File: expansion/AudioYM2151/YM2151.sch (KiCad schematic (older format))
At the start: 17 parts, among them U3 LTC690x, U4 YM2151, U5 YM3012, U6 TL064

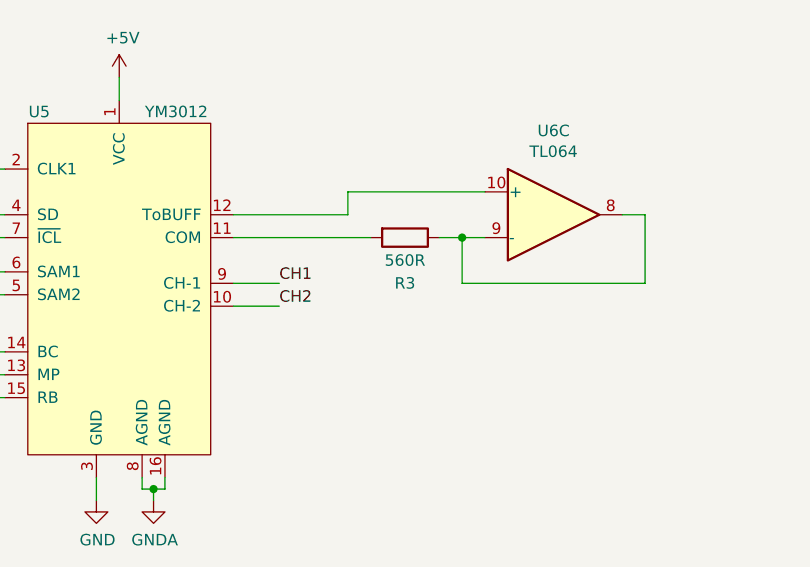
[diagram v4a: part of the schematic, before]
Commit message: Re-started layout on YM2151 board
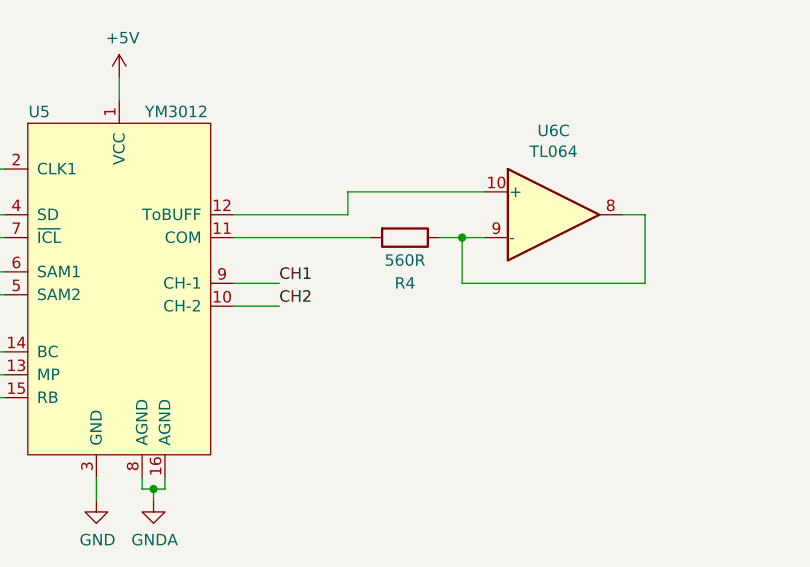
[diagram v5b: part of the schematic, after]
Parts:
- renumbered R3 to R4
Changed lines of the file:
@@
 $EndComp
 $Comp
-L Device:R R3
+L Device:R R4
 U 1 1 60BAB26A
 P 7800 4550
-F 0 "R3" V 8000 4550 50  0000 C CNN
+F 0 "R4" V 8000 4550 50  0000 C CNN
 F 1 "560R" V 7900 4550 50  0000 C CNN
 F 2 "Resistor_THT:R_Axial_DIN0207_L6.3mm_D2.5mm_P10.16mm_Horizontal" V 7730 4550 50  0001 C CNN
@@
 	2050 5450 2300 5450
 $Comp
-L power:+5V #PWR030
+L power:+5V #PWR031
 U 1 1 60C08870
 P 2750 3800
-F 0 "#PWR030" H 2750 3650 50  0001 C CNN
+F 0 "#PWR031" H 2750 3650 50  0001 C CNN
 F 1 "+5V" H 2765 3973 50  0000 C CNN
 F 2 "" H 2750 3800 50  0001 C CNN
@@
 $EndComp
 $Comp
-L power:GND #PWR031
+L power:GND #PWR032
 U 1 1 60C08E24
 P 2750 5850
-F 0 "#PWR031" H 2750 5600 50  0001 C CNN
+F 0 "#PWR032" H 2750 5600 50  0001 C CNN
 F 1 "GND" H 2755 5677 50  0000 C CNN
 F 2 "" H 2750 5850 50  0001 C CNN
@@
 $EndComp
 $Comp
-L power:GND #PWR040
+L power:GND #PWR041
 U 1 1 60C0A870
 P 6450 5700
-F 0 "#PWR040" H 6450 5450 50  0001 C CNN
+F 0 "#PWR041" H 6450 5450 50  0001 C CNN
 F 1 "GND" H 6455 5527 50  0000 C CNN
 F 2 "" H 6450 5700 50  0001 C CNN
@@
 	2750 5800 2800 5800
 $Comp
-L power:+5V #PWR041
+L power:+5V #PWR042
 U 1 1 60C9B598
 P 6550 3850
-F 0 "#PWR041" H 6550 3700 50  0001 C CNN
+F 0 "#PWR042" H 6550 3700 50  0001 C CNN
 F 1 "+5V" H 6565 4023 50  0000 C CNN
 F 2 "" H 6550 3850 50  0001 C CNN
@@
 $EndComp
 $Comp
-L power:+5V #PWR028
+L power:+5V #PWR029
 U 1 1 60CD204F
 P 2750 2000
-F 0 "#PWR028" H 2750 1850 50  0001 C CNN
+F 0 "#PWR029" H 2750 1850 50  0001 C CNN
 F 1 "+5V" H 2765 2173 50  0000 C CNN
 F 2 "" H 2750 2000 50  0001 C CNN
@@
 $EndComp
 $Comp
-L power:GND #PWR029
+L power:GND #PWR030
 U 1 1 60CD264A
 P 2750 3200
-F 0 "#PWR029" H 2750 2950 50  0001 C CNN
+F 0 "#PWR030" H 2750 2950 50  0001 C CNN
 F 1 "GND" H 2755 3027 50  0000 C CNN
 F 2 "" H 2750 3200 50  0001 C CNN
@@
 	5100 4250 6050 4250
 $Comp
-L power:+5V #PWR036
+L power:+5V #PWR037
 U 1 1 60D62AD7
 P 4700 3250
-F 0 "#PWR036" H 4700 3100 50  0001 C CNN
+F 0 "#PWR037" H 4700 3100 50  0001 C CNN
 F 1 "+5V" H 4715 3423 50  0000 C CNN
 F 2 "" H 4700 3250 50  0001 C CNN
@@
 $EndComp
 $Comp
-L power:GND #PWR033
+L power:GND #PWR034
 U 1 1 6153751F
 P 3300 3200
-F 0 "#PWR033" H 3300 2950 50  0001 C CNN
+F 0 "#PWR034" H 3300 2950 50  0001 C CNN
 F 1 "GND" H 3305 3027 50  0000 C CNN
 F 2 "" H 3300 3200 50  0001 C CNN
@@
 $EndComp
 $Comp
-L power:+5V #PWR032
+L power:+5V #PWR033
 U 1 1 61537D3F
 P 3300 2000
-F 0 "#PWR032" H 3300 1850 50  0001 C CNN
+F 0 "#PWR033" H 3300 1850 50  0001 C CNN
 F 1 "+5V" H 3315 2173 50  0000 C CNN
 F 2 "" H 3300 2000 50  0001 C CNN
@@
 	3300 2700 3300 2800
 $Comp
-L power:GNDA #PWR042
+L power:GNDA #PWR043
 U 1 1 61042847
 P 6700 5700
-F 0 "#PWR042" H 6700 5450 50  0001 C CNN
+F 0 "#PWR043" H 6700 5450 50  0001 C CNN
 F 1 "GNDA" H 6705 5527 50  0000 C CNN
 F 2 "" H 6700 5700 50  0001 C CNN
@@
 $EndComp
 $Comp
-L power:GNDA #PWR046
+L power:GNDA #PWR047
 U 1 1 61042C03
 P 9700 5750
-F 0 "#PWR046" H 9700 5500 50  0001 C CNN
+F 0 "#PWR047" H 9700 5500 50  0001 C CNN
 F 1 "GNDA" H 9705 5577 50  0000 C CNN
 F 2 "" H 9700 5750 50  0001 C CNN
@@
 $EndComp
 $Comp
-L power:GNDA #PWR043
+L power:GNDA #PWR044
 U 1 1 610435DB
 P 8150 1750
-F 0 "#PWR043" H 8150 1500 50  0001 C CNN
+F 0 "#PWR044" H 8150 1500 50  0001 C CNN
 F 1 "GNDA" H 8155 1577 50  0000 C CNN
 F 2 "" H 8150 1750 50  0001 C CNN
@@
 $EndComp
 $Comp
-L power:GNDA #PWR044
+L power:GNDA #PWR045
 U 1 1 61043A6E
 P 8150 3050
-F 0 "#PWR044" H 8150 2800 50  0001 C CNN
+F 0 "#PWR045" H 8150 2800 50  0001 C CNN
 F 1 "GNDA" H 8155 2877 50  0000 C CNN
 F 2 "" H 8150 3050 50  0001 C CNN
@@
 $EndComp
 $Comp
-L power:GNDA #PWR039
+L power:GNDA #PWR040
 U 1 1 61043CBD
 P 5750 2350
-F 0 "#PWR039" H 5750 2100 50  0001 C CNN
+F 0 "#PWR040" H 5750 2100 50  0001 C CNN
 F 1 "GNDA" H 5755 2177 50  0000 C CNN
 F 2 "" H 5750 2350 50  0001 C CNN
@@
 	3650 6450 3650 6550
 $Comp
-L power:GNDA #PWR035
+L power:GNDA #PWR036
 U 1 1 61044112
 P 3650 7150
-F 0 "#PWR035" H 3650 6900 50  0001 C CNN
+F 0 "#PWR036" H 3650 6900 50  0001 C CNN
 F 1 "GNDA" H 3655 6977 50  0000 C CNN
 F 2 "" H 3650 7150 50  0001 C CNN
@@
 P 5350 7150
 AR Path="/60D530A5/60EA6620" Ref="#PWR?"  Part="1"
-AR Path="/60B0BE0A/60EA6620" Ref="#PWR038"  Part="1"
-F 0 "#PWR038" H 5350 6900 50  0001 C CNN
+AR Path="/60B0BE0A/60EA6620" Ref="#PWR039"  Part="1"
+F 0 "#PWR039" H 5350 6900 50  0001 C CNN
 F 1 "GND" H 5355 6977 50  0000 C CNN
 F 2 "" H 5350 7150 50  0001 C CNN
@@
 P 5350 6450
 AR Path="/60D530A5/60EA6626" Ref="#PWR?"  Part="1"
-AR Path="/60B0BE0A/60EA6626" Ref="#PWR037"  Part="1"
-F 0 "#PWR037" H 5350 6300 50  0001 C CNN
+AR Path="/60B0BE0A/60EA6626" Ref="#PWR038"  Part="1"
+F 0 "#PWR038" H 5350 6300 50  0001 C CNN
 F 1 "+5V" H 5365 6623 50  0000 C CNN
 F 2 "" H 5350 6450 50  0001 C CNN
@@
 P 3650 6450
 AR Path="/60D530A5/6115823E" Ref="#PWR?"  Part="1"
-AR Path="/60B0BE0A/6115823E" Ref="#PWR0101"  Part="1"
-F 0 "#PWR0101" H 3650 6300 50  0001 C CNN
+AR Path="/60B0BE0A/6115823E" Ref="#PWR035"  Part="1"
+F 0 "#PWR035" H 3650 6300 50  0001 C CNN
 F 1 "+5V" H 3665 6623 50  0000 C CNN
 F 2 "" H 3650 6450 50  0001 C CNN
@@
 P 9700 4950
 AR Path="/60D530A5/61158651" Ref="#PWR?"  Part="1"
-AR Path="/60B0BE0A/61158651" Ref="#PWR0102"  Part="1"
-F 0 "#PWR0102" H 9700 4800 50  0001 C CNN
+AR Path="/60B0BE0A/61158651" Ref="#PWR046"  Part="1"
+F 0 "#PWR046" H 9700 4800 50  0001 C CNN
 F 1 "+5V" H 9715 5123 50  0000 C CNN
 F 2 "" H 9700 4950 50  0001 C CNN

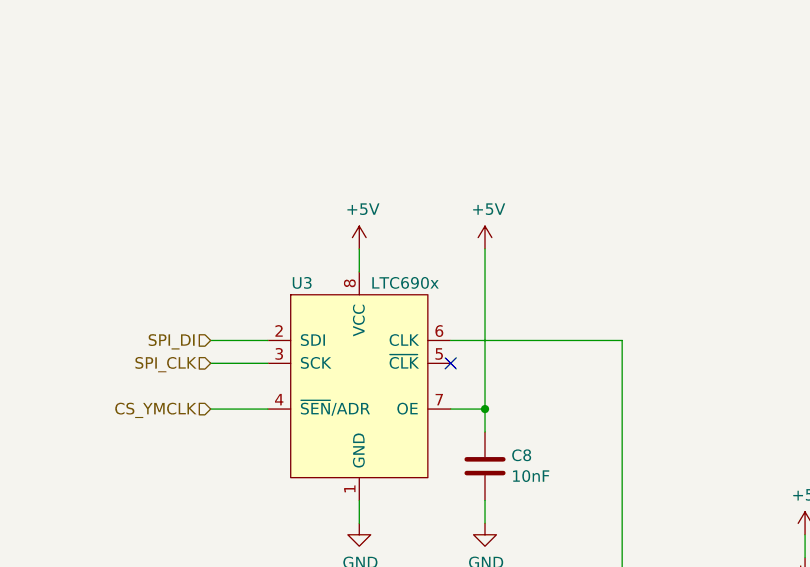
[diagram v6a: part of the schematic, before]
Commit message: Added V9958 CPLD code
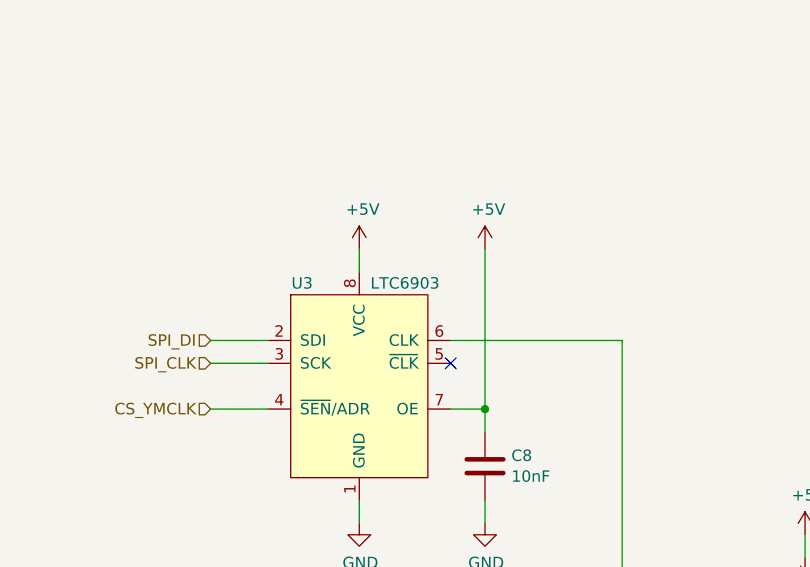
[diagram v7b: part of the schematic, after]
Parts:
- U3: value LTC690x -> LTC6903
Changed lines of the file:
@@
 P 2750 2750
 F 0 "U3" H 2500 3350 50  0000 C CNN
-F 1 "LTC690x" H 2950 3350 50  0000 C CNN
+F 1 "LTC6903" H 2950 3350 50  0000 C CNN
 F 2 "Package_SO:MSOP-8_3x3mm_P0.65mm" H 2750 2750 50  0001 C CNN
 F 3 "" H 2750 2750 50  0001 C CNN
